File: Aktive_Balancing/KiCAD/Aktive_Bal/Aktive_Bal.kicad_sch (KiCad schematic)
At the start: 59 parts, among them J16 Conn_01x02_Pin, J17 Conn_01x02_Pin, J18 Conn_01x02_Pin, J19 Conn_01x02_Pin, J2 Sockel_BluePill, J20 Conn_01x02_Pin, J21 Conn_01x02_Pin, J3 A-DF_09_A_KG-T4S, J4 Screw_Terminal_01x02, J9 Conn_01x01_Pin, U1 SCW20C-12, U13 RFP12N10L, U14 PCF8575CDB, U15 SN65HVD233, U2 EC1SA16N, U5 ADUM1250ARZ-RL7, U6 PCA9306DC, U7 LM1117IMPX_3_3_NOPB, U8 MCP4725xxx-xCH

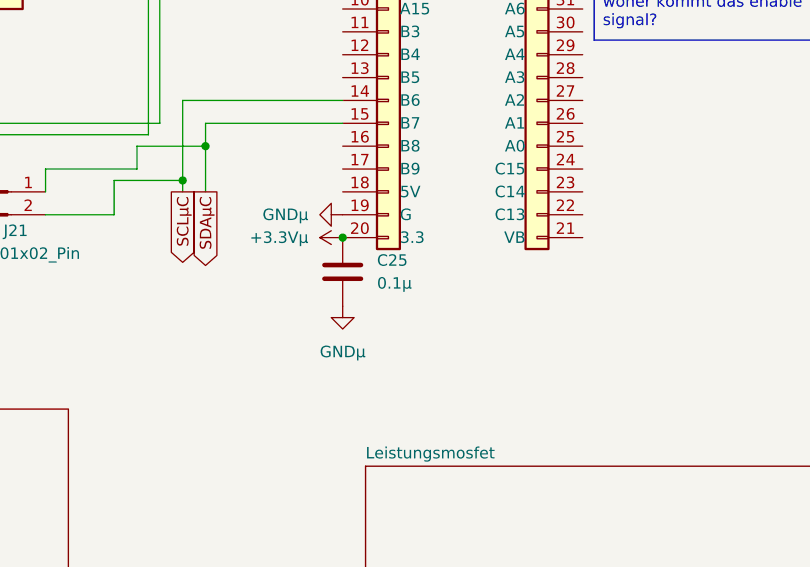
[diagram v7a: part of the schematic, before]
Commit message: kondensator an den 3.3V µc
den kondensator an der Stiftleiste vom mikrokontroller geändert zu einem Bulk kondensator
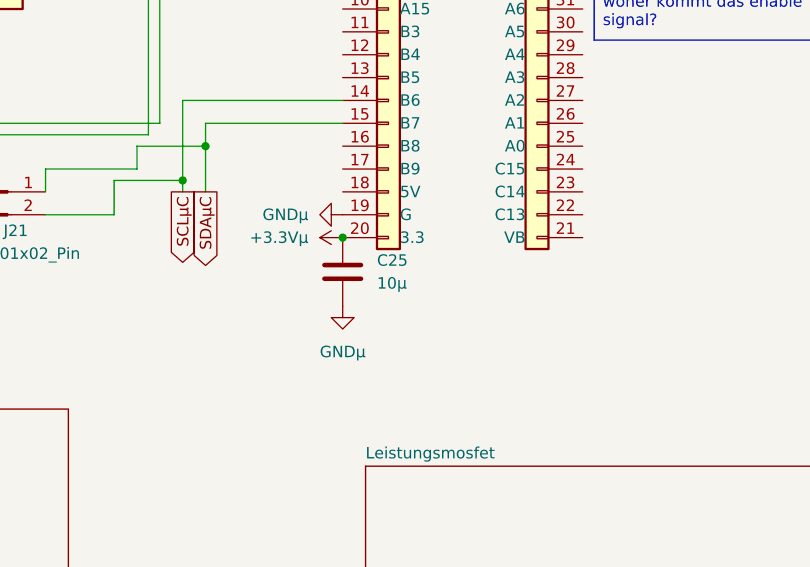
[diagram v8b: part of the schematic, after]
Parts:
- C25: value 0.1µ -> 10µ
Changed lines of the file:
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@@
 			)
 		)
-		(property "Value" "0.1µ"
+		(property "Value" "10µ"
 			(at 114.3 190.4999 0)
 			(show_name no)
